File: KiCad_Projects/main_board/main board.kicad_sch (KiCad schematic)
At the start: 63 parts

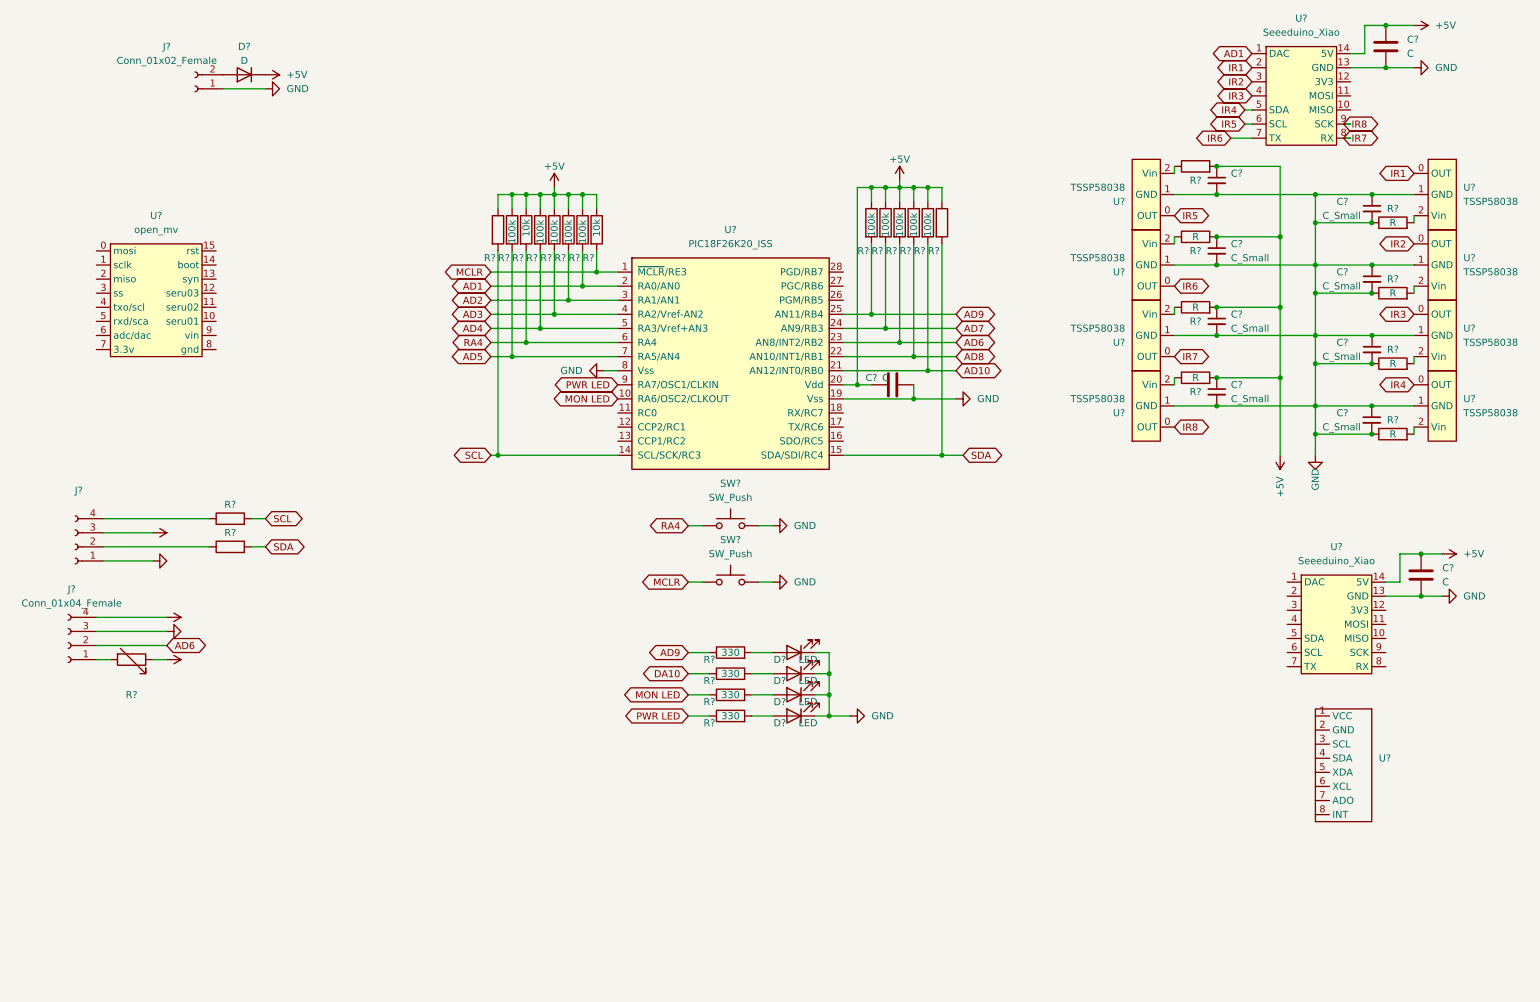
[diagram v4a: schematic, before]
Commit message: 基板の更新
メイン基板の更新、ライブラリの追加
※電源基盤はいまだ理解できずに手が付けられてない。
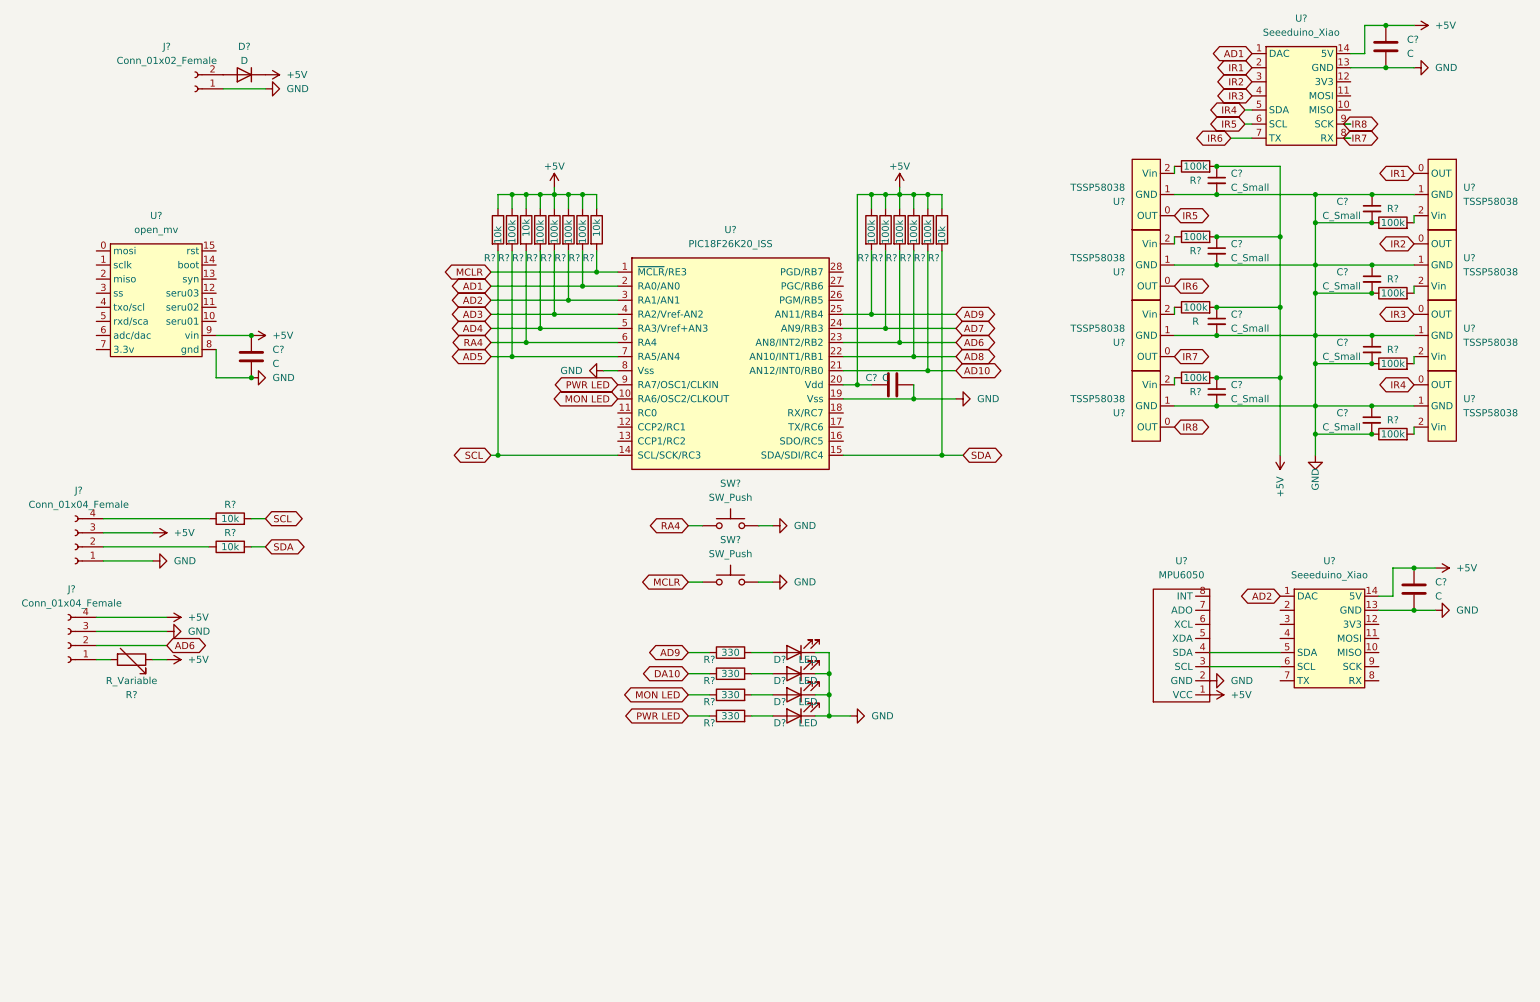
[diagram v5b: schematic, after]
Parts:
- added C?: C, symbol Device:C
- C?: value (none) -> C_Small
- J?: value (none) -> Conn_01x04_Female
- R: renamed from R?; value R -> 100k
- R? (x6): value R -> 100k
- R? (x4): value (none) -> 10k
- R?: value (none) -> R_Variable
- R?: value (none) -> 100k
- U?: value (none) -> MPU6050
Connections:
- net +5V: now also U?.1 (VCC), U?.9 (vin), C?.1
- net AD2: now also U?.1 (DAC)
- net GND: now also U?.2 (GND), U?.8 (gnd), C?.2
- net at U?.3 (SCL): now also U?.6 (SCL)
- net at U?.4 (SDA): now also U?.5 (SDA)
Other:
- moved on the sheet: C?, R?, U?

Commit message: 基盤データの更新　
メイン基板の回路図の更新
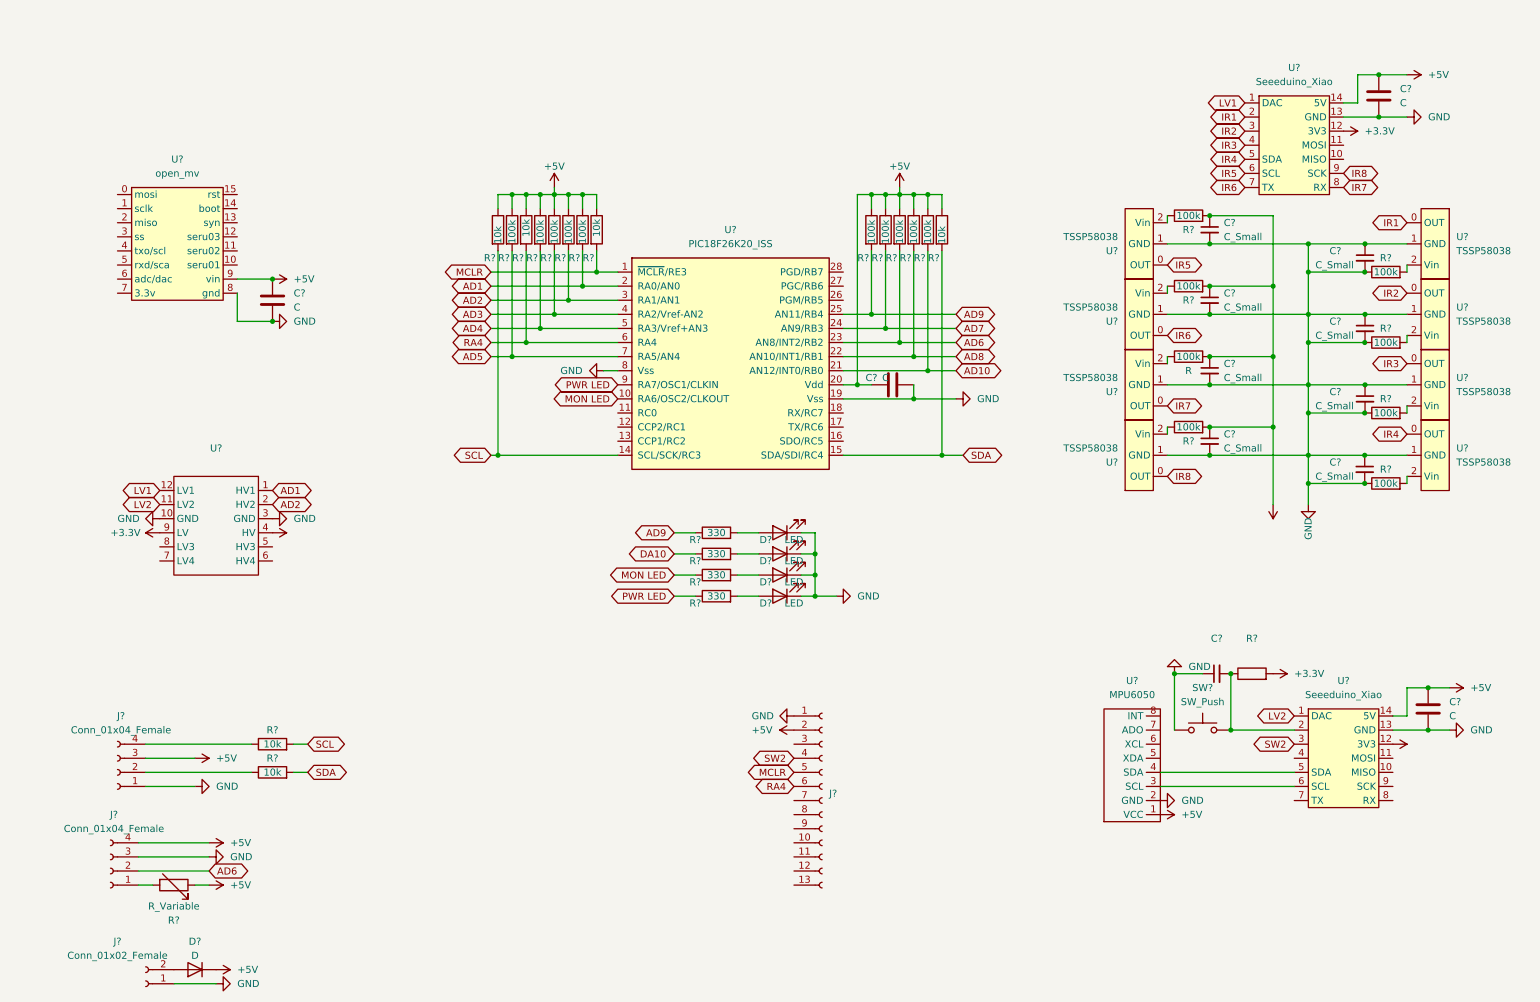
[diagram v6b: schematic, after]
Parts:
- removed SW? (x2): SW_Push, symbol Switch:SW_Push
- added C?: (no value), symbol Device:C_Small
- added J?: (no value), symbol Connector:Conn_01x13_Female
- added R?: (no value), symbol Device:R
- added SW?: SW_Push, symbol Switch:SW_Push
- added U?: (no value), symbol Logic_Level_Converter:Akizuki_Logiv_Level_converter
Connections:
- net +5V: now also J?.2 (Pin_2), U?.4 (HV); no longer C?.1, C?.1, C?.1, C?.1, R.2, R?.2, R?.2, R?.2
- net AD1: now also U?.1 (HV1); no longer U?.1 (DAC)
- net AD2: now also U?.2 (HV2); no longer U?.1 (DAC)
- net GND: now also C?.1, J?.1 (Pin_1), SW?.1, U?.10 (GND), U?.3 (GND)
- net MCLR: now also J?.5 (Pin_5)
- net RA4: now also J?.6 (Pin_6)
- net +3V3: now reaches U?.12 (3V3)
- net +3V3: now also C?.1, C?.1, C?.1, C?.1, R.2, R?.2, R?.2, R?.2, U?.12 (3V3), R?.2, U?.9 (LV)
- net at U?.2: now also C?.2, R?.1, SW?.2
- net SW2: now reaches U?.3
- net SW2: now also J?.4 (Pin_4)
- new net LV1: U?.1 (DAC), U?.12 (LV1)
- new net LV2: U?.1 (DAC), U?.11 (LV2)
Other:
- moved on the sheet: C?, D?, J?, R, R?, U?

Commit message: 基盤データのアップデート
ローカルコミットはちゃんと作ってください
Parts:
- removed J?: (no value), symbol Connector:Conn_01x13_Female
- added J?: Conn_01x05_Female, symbol Connector:Conn_01x05_Female
- C?: value (none) -> C_Small
- R?: value (none) -> R
- U?: value (none) -> Akizuki_Logiv_Level_converter
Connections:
- net +5V: now also J?.2 (Pin_2)
- net GND: now also J?.1 (Pin_1)
- net MCLR: now also J?.4 (Pin_4)
- net RA4: now also J?.5 (Pin_5)
- net SW2: now also J?.3 (Pin_3)
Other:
- moved on the sheet: C?, D?, J?, R?, U?

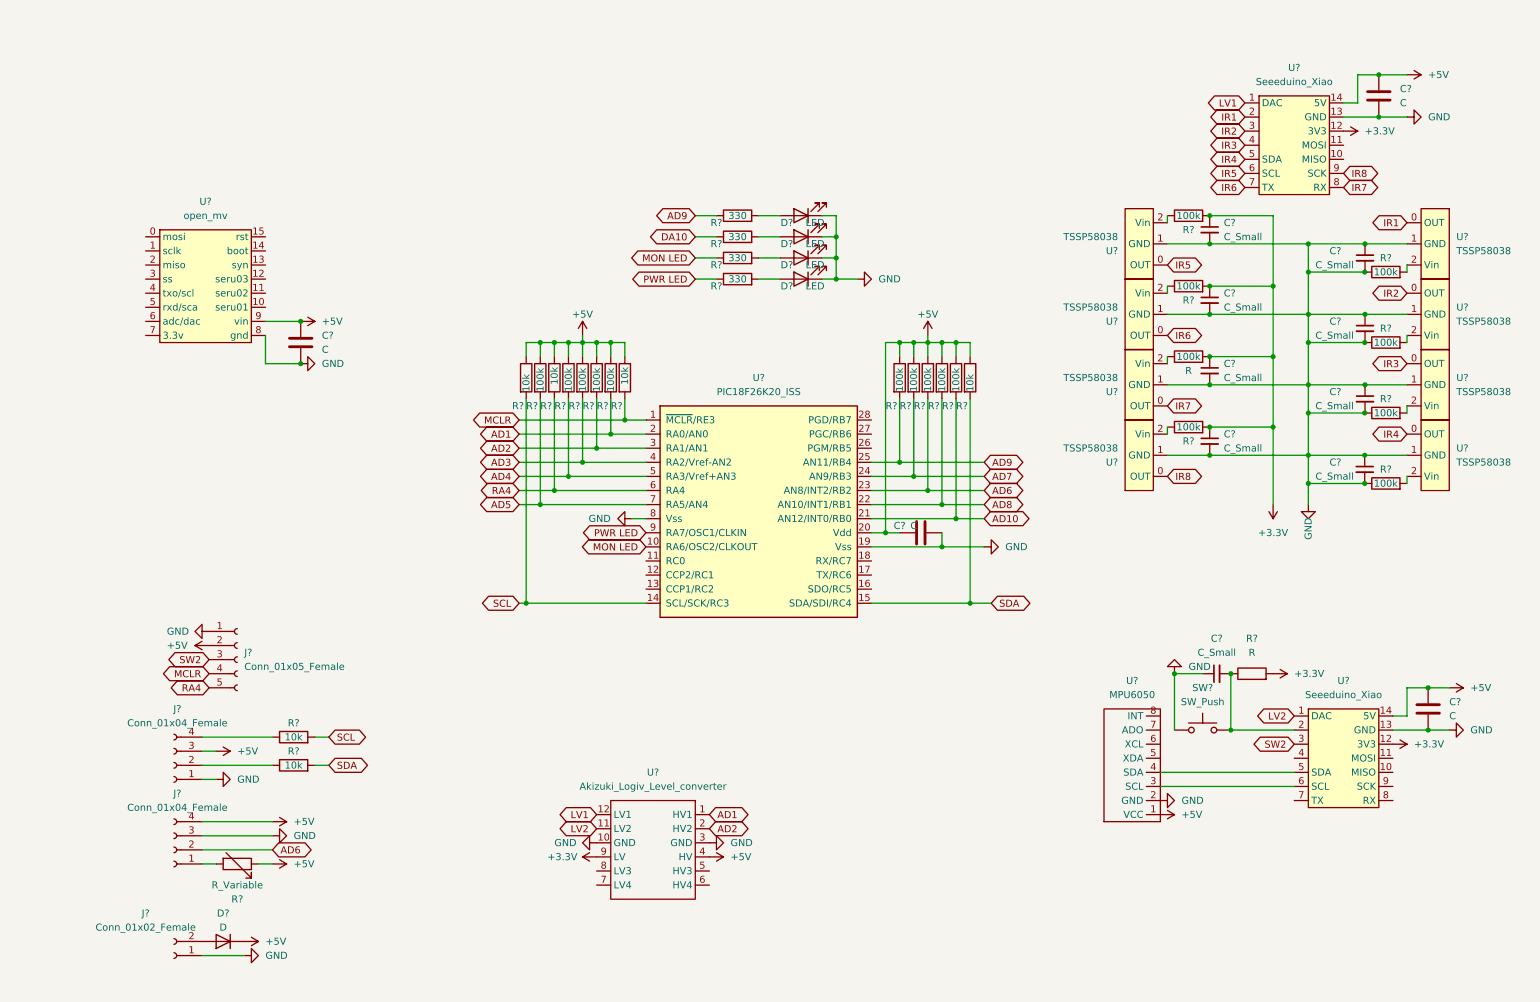
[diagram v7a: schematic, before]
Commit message: 基板データの更新
ラインセンサーの完成
Arduino メイン基板の作成、製作開始。
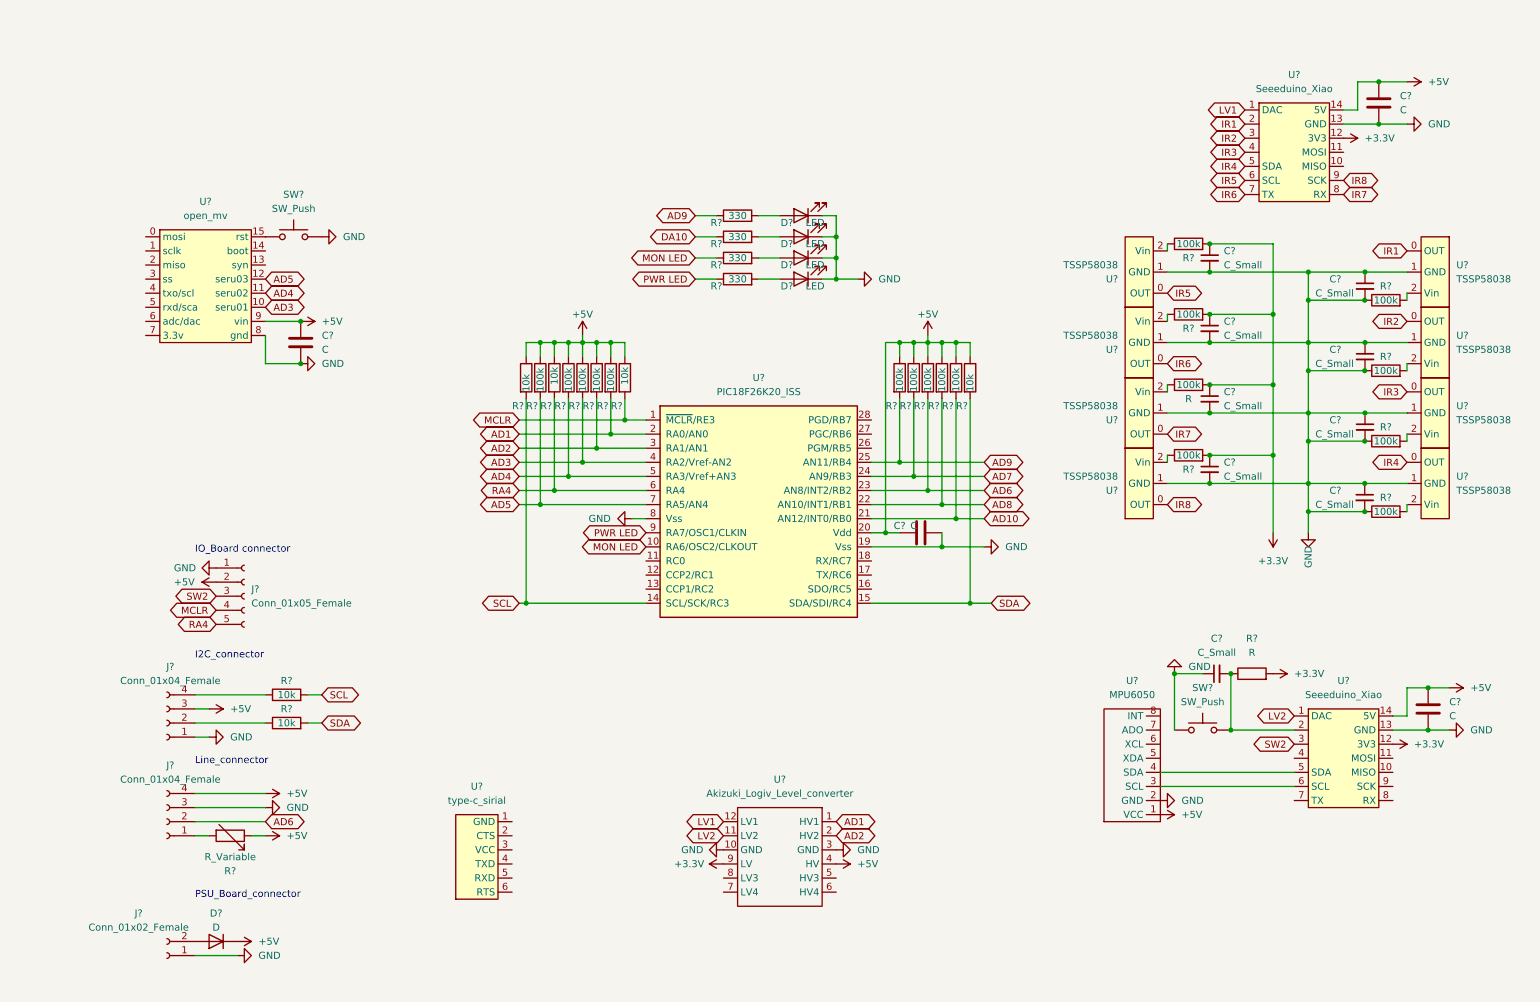
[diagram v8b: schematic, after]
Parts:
- added SW?: SW_Push, symbol Switch:SW_Push
- added U?: type-c_sirial, symbol type-c_sirial:type-c_sirial
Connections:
- net AD3: now also U?.10 (seru01)
- net AD4: now also U?.11 (seru02)
- net AD5: now also U?.12 (seru03)
- net GND: now also SW?.2
- net at U?.15 (rst): now also SW?.1
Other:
- note added: "I2C_connector"
- note added: "IO_Board connector"
- note added: "Line_connector"
- note added: "PSU_Board_connector"
- moved on the sheet: C?, D?, J?, R, R?, U?
